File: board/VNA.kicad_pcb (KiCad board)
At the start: 2 copper layers, 100 x 100 mm, 129 parts, among them J1 Conn_02x05_Odd_Even, J10 Conn_01x01, J11 Conn_01x01, J12 Conn_01x01, J13 Barrel_Jack, J15 Conn_02x05_Odd_Even, J17 Conn_01x04, J18 Conn_01x01, J19 Conn_01x01, J2 Conn_Coaxial, J20 Conn_01x01, J21 Conn_01x01, J22 Conn_01x02, J3 Conn_01x01, J4 Conn_01x01, J5 Conn_01x01, J6 Conn_01x01, J7 Conn_01x01, J8 Conn_01x01, J9 Conn_Coaxial, Q1 SS9018, U1 SI5351A, U2 LM339, U3 SA612, U4 SA612, U5 SA612, U6 TL082, U7 TL082, U9 LM7805_TO220, Y1 27 MHz

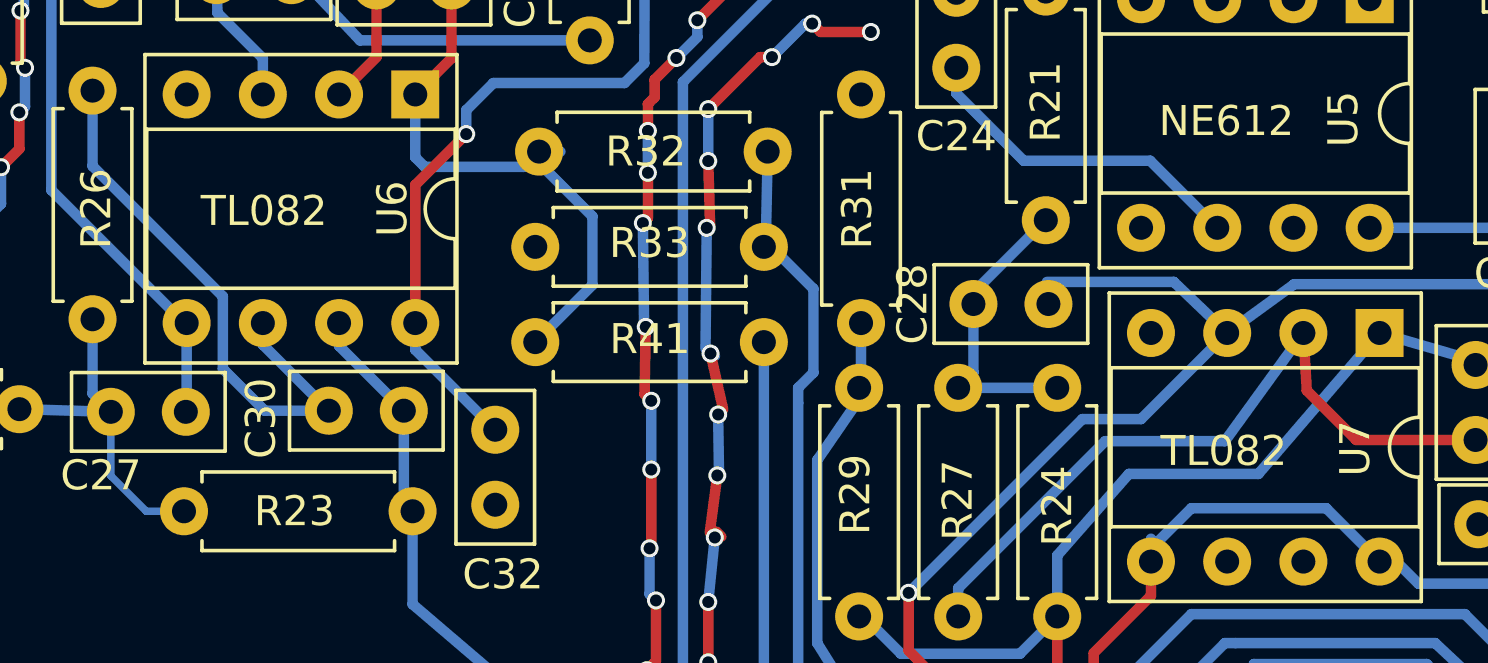
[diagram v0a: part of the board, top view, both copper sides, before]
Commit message: Changed TL082 to LM358, other corrections to software
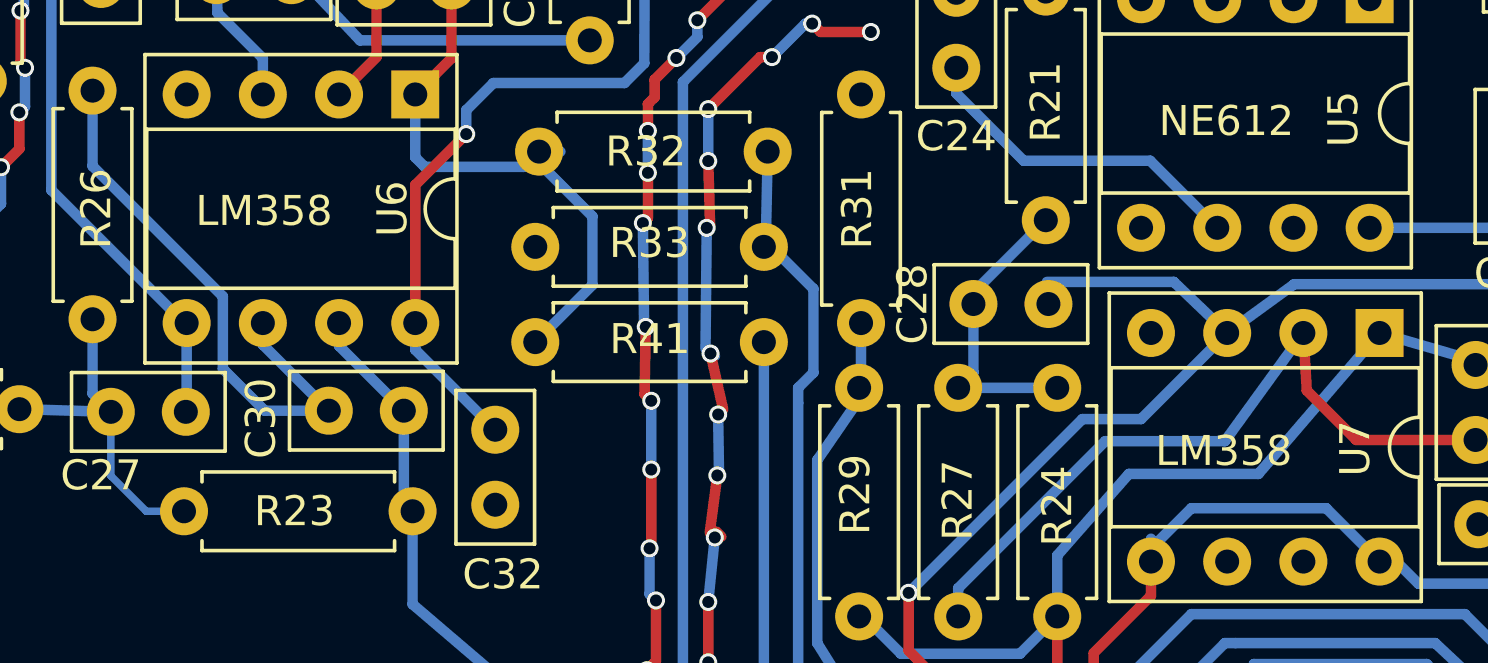
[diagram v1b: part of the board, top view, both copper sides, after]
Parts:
- R3: value 470R -> 1k
- R4: value 470R -> 680R
- R42: value 10k -> 1k
- U6, U7: value TL082 -> LM358
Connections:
- net 2V5 renamed 2V0
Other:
- board text added: "LM358"
- board text removed: "TL082"

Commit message: A few minor fixes, grounding, etc.
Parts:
- moved U9 4.05 mm to (145.9, 121.0)
- moved C38 0.56 mm to (145.8, 111.1)
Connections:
- J18 pad 1: (no net) -> GND
- J19 pad 1: (no net) -> GND
- J20 pad 1: (no net) -> GND
- J21 pad 1: (no net) -> GND
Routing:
- net +5V: track 310.8 -> 317.6 mm
- net Net-(C47-Pad1): track 43.3 -> 47.0 mm

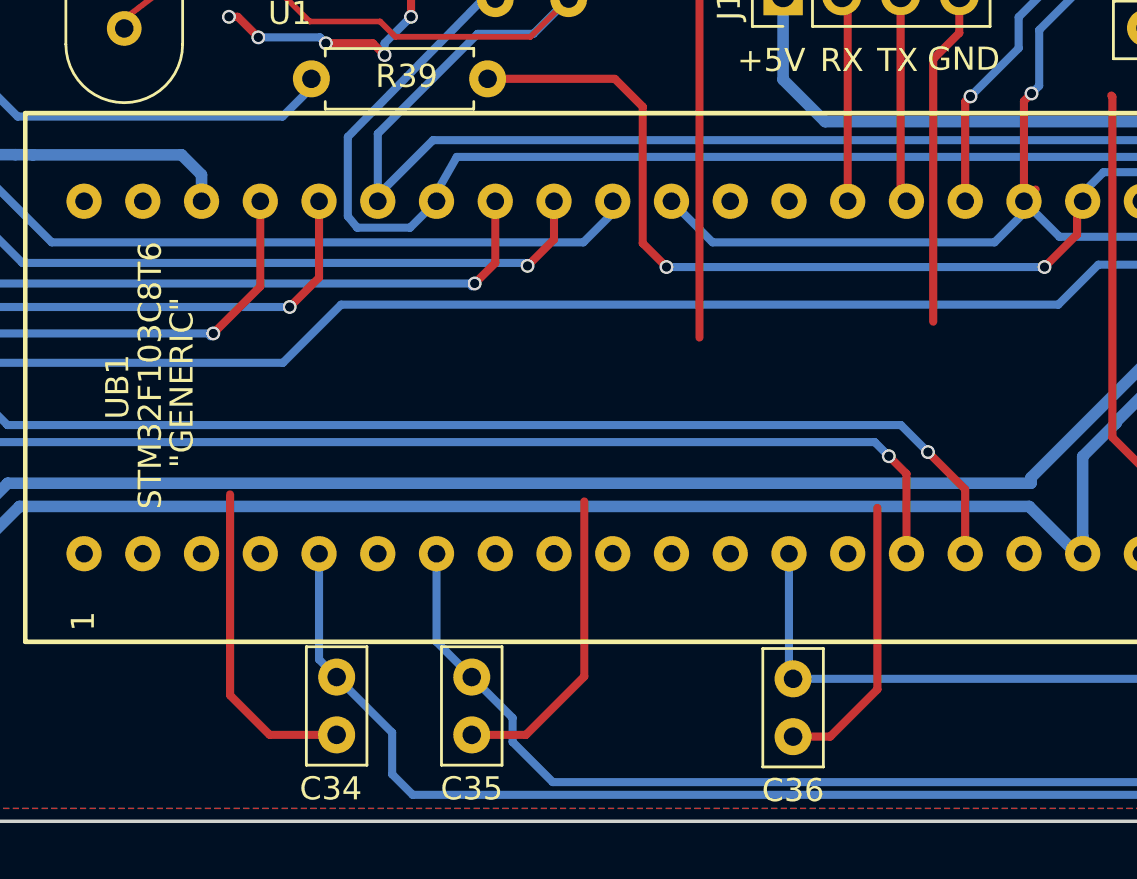
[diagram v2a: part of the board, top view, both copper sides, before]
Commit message: Added ground connections
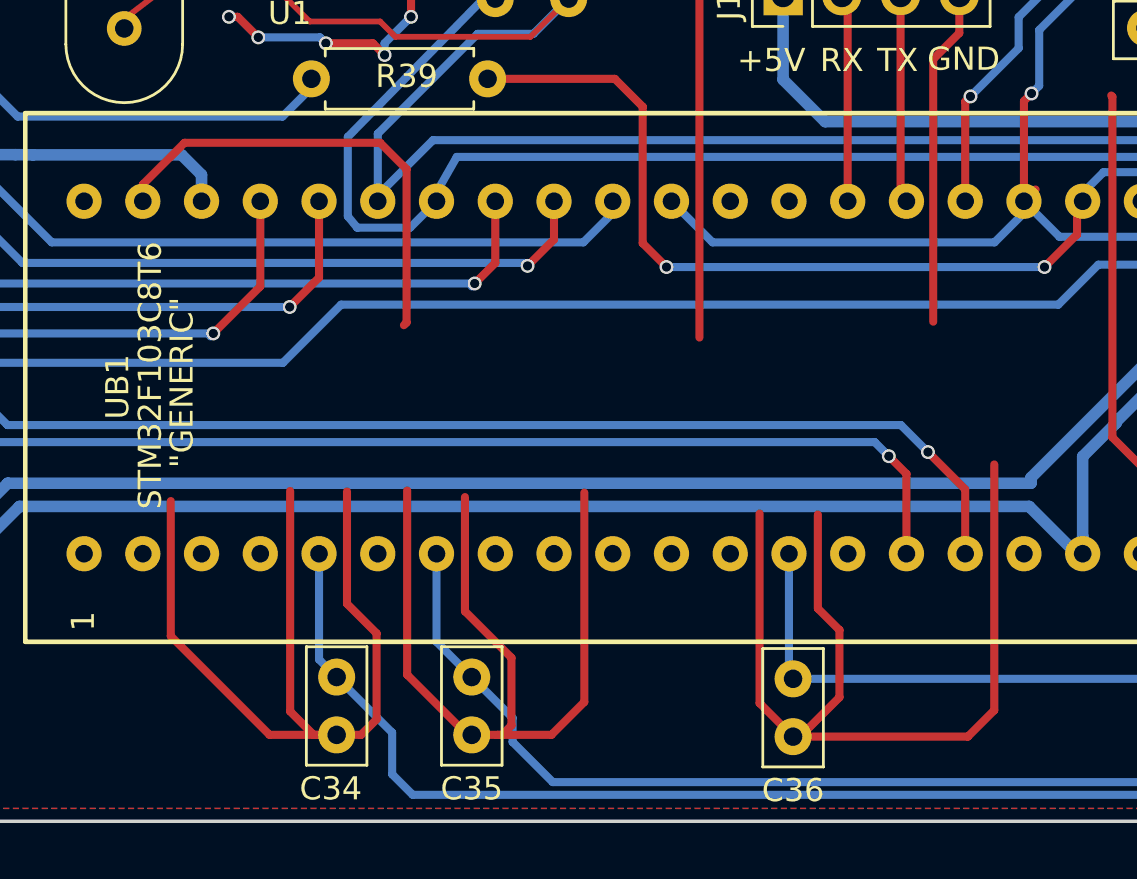
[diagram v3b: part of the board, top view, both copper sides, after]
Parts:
- R16: value 100R -> 51R
- R40: value NC -> 100R
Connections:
- UB1 pad 71: (no net) -> GND
- UB1 pad 74: (no net) -> GND
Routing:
- net GND: track 610.7 -> 709.1 mm
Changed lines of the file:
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@@
 (kicad_pcb (version 4) (host pcbnew 4.0.7)
   (general
-    (links 247)
+    (links 249)
     (no_connects 0)
     (area 48.252381 29.036639 153.343482 154.699701)
     (thickness 1.6)
     (drawings 35)
-    (tracks 1485)
+    (tracks 1515)
     (zones 0)
     (modules 129)
@@
   )
   (setup
-    (last_trace_width 0.25)
+    (last_trace_width 0.35)
     (user_trace_width 0.35)
     (user_trace_width 0.5)
@@
       (effects (font (size 1 1) (thickness 0.15)))
     )
-    (fp_text value 100R (at 3.81 2.31 270) (layer F.Fab)
+    (fp_text value 51R (at 3.81 2.31 270) (layer F.Fab)
       (effects (font (size 1 1) (thickness 0.15)))
     )
@@
     (pad 70 thru_hole circle (at -7.62 21.59 90) (size 1.524 1.524) (drill 0.762) (layers *.Cu *.Mask)
       (net 46 +3V3))
-    (pad 71 thru_hole circle (at -7.62 24.13 90) (size 1.524 1.524) (drill 0.762) (layers *.Cu *.Mask))
+    (pad 71 thru_hole circle (at -7.62 24.13 90) (size 1.524 1.524) (drill 0.762) (layers *.Cu *.Mask)
+      (net 2 GND))
     (pad 72 thru_hole circle (at -7.62 26.67 90) (size 1.524 1.524) (drill 0.762) (layers *.Cu *.Mask)
       (net 2 GND))
     (pad 73 thru_hole circle (at 7.62 -21.59 90) (size 1.524 1.524) (drill 0.762) (layers *.Cu *.Mask))
-    (pad 74 thru_hole circle (at 7.62 -19.05 90) (size 1.524 1.524) (drill 0.762) (layers *.Cu *.Mask))
+    (pad 74 thru_hole circle (at 7.62 -19.05 90) (size 1.524 1.524) (drill 0.762) (layers *.Cu *.Mask)
+      (net 2 GND))
     (pad 75 thru_hole circle (at 7.62 -16.51 90) (size 1.524 1.524) (drill 0.762) (layers *.Cu *.Mask)
       (net 45 +5V))
@@
       (effects (font (size 1 1) (thickness 0.15)))
     )
-    (fp_text value NC (at 3.81 2.31) (layer F.Fab)
+    (fp_text value 100R (at 3.81 2.31) (layer F.Fab)
       (effects (font (size 1 1) (thickness 0.15)))
     )
@@
   (segment (start 144.5768 76.962) (end 145.796 76.962) (width 0.5) (layer B.Cu) (net 1) (status 20))
   (segment (start 142.6464 78.8924) (end 144.5768 76.962) (width 0.5) (layer B.Cu) (net 1))
-  (segment (start 80.264 146.264) (end 77.36904 146.264) (width 0.35) (layer F.Cu) (net 2))
-  (segment (start 75.65644 144.5514) (end 75.65644 135.8646) (width 0.35) (layer F.Cu) (net 2))
-  (segment (start 77.36904 146.264) (end 75.65644 144.5514) (width 0.35) (layer F.Cu) (net 2))
-  (segment (start 99.9998 146.3402) (end 101.60444 146.3402) (width 0.35) (layer F.Cu) (net 2))
-  (segment (start 103.64724 144.2974) (end 103.64724 136.4488) (width 0.35) (layer F.Cu) (net 2))
-  (segment (start 101.60444 146.3402) (end 103.64724 144.2974) (width 0.35) (layer F.Cu) (net 2))
-  (segment (start 86.106 146.264) (end 88.44724 146.264) (width 0.35) (layer F.Cu) (net 2))
-  (segment (start 90.97264 143.7386) (end 90.97264 136.1694) (width 0.35) (layer F.Cu) (net 2))
-  (segment (start 88.44724 146.264) (end 90.97264 143.7386) (width 0.35) (layer F.Cu) (net 2))
+  (segment (start 71.882 123.19) (end 71.882 122.4661) (width 0.35) (layer F.Cu) (net 2))
+  (segment (start 71.882 122.4661) (end 73.6854 120.6627) (width 0.35) (layer F.Cu) (net 2))
+  (segment (start 73.6854 120.6627) (end 82.1436 120.6627) (width 0.35) (layer F.Cu) (net 2))
+  (segment (start 82.1436 120.6627) (end 83.2866 121.8057) (width 0.35) (layer F.Cu) (net 2))
+  (segment (start 83.2866 121.8057) (end 83.2866 128.4351) (width 0.35) (layer F.Cu) (net 2))
+  (segment (start 83.2866 128.4351) (end 83.1723 128.5494) (width 0.35) (layer F.Cu) (net 2))
+  (segment (start 80.264 146.264) (end 77.36396 146.264) (width 0.35) (layer F.Cu) (net 2))
+  (segment (start 73.09104 141.99108) (end 73.09104 136.15162) (width 0.35) (layer F.Cu) (net 2))
+  (segment (start 77.36396 146.264) (end 73.09104 141.99108) (width 0.35) (layer F.Cu) (net 2))
+  (segment (start 99.9998 146.3402) (end 107.5582 146.3402) (width 0.35) (layer F.Cu) (net 2))
+  (segment (start 108.6993 145.1991) (end 108.6993 134.5692) (width 0.35) (layer F.Cu) (net 2))
+  (segment (start 107.5582 146.3402) (end 108.6993 145.1991) (width 0.35) (layer F.Cu) (net 2))
+  (segment (start 87.20074 146.264) (end 89.5496 146.264) (width 0.35) (layer F.Cu) (net 2))
+  (segment (start 90.97264 144.84096) (end 90.97264 135.7884) (width 0.35) (layer F.Cu) (net 2))
+  (segment (start 89.5496 146.264) (end 90.97264 144.84096) (width 0.35) (layer F.Cu) (net 2))
+  (segment (start 99.9998 146.3402) (end 100.30396 146.3402) (width 0.35) (layer F.Cu) (net 2))
+  (segment (start 100.30396 146.3402) (end 102.0064 144.63776) (width 0.35) (layer F.Cu) (net 2))
+  (segment (start 101.07168 140.79728) (end 101.07168 136.73328) (width 0.35) (layer F.Cu) (net 2))
+  (segment (start 102.0064 141.732) (end 101.07168 140.79728) (width 0.35) (layer F.Cu) (net 2))
+  (segment (start 102.0064 144.63776) (end 102.0064 141.732) (width 0.35) (layer F.Cu) (net 2))
+  (segment (start 98.552 136.69264) (end 98.552 144.8924) (width 0.35) (layer F.Cu) (net 2))
+  (segment (start 98.552 144.8924) (end 99.9998 146.3402) (width 0.35) (layer F.Cu) (net 2))
+  (segment (start 85.81136 135.98144) (end 85.81136 140.9192) (width 0.35) (layer F.Cu) (net 2))
+  (segment (start 87.416 146.264) (end 87.20074 146.264) (width 0.35) (layer F.Cu) (net 2))
+  (segment (start 87.20074 146.264) (end 86.106 146.264) (width 0.35) (layer F.Cu) (net 2))
+  (segment (start 87.82304 145.85696) (end 87.416 146.264) (width 0.35) (layer F.Cu) (net 2))
+  (segment (start 87.82304 142.93088) (end 87.82304 145.85696) (width 0.35) (layer F.Cu) (net 2))
+  (segment (start 85.81136 140.9192) (end 87.82304 142.93088) (width 0.35) (layer F.Cu) (net 2))
+  (segment (start 86.106 146.264) (end 85.9136 146.264) (width 0.35) (layer F.Cu) (net 2))
+  (segment (start 85.9136 146.264) (end 83.312 143.6624) (width 0.35) (layer F.Cu) (net 2))
+  (segment (start 83.312 143.6624) (end 83.312 135.69696) (width 0.35) (layer F.Cu) (net 2))
+  (segment (start 80.264 146.264) (end 81.32 146.264) (width 0.35) (layer F.Cu) (net 2))
+  (segment (start 80.71104 140.59408) (end 80.71104 135.7376) (width 0.35) (layer F.Cu) (net 2))
+  (segment (start 81.9912 141.87424) (end 80.71104 140.59408) (width 0.35) (layer F.Cu) (net 2))
+  (segment (start 81.9912 145.5928) (end 81.9912 141.87424) (width 0.35) (layer F.Cu) (net 2))
+  (segment (start 81.32 146.264) (end 81.9912 145.5928) (width 0.35) (layer F.Cu) (net 2))
+  (segment (start 80.264 146.264) (end 79.26896 146.264) (width 0.35) (layer F.Cu) (net 2))
+  (segment (start 78.25232 145.24736) (end 78.25232 135.71728) (width 0.35) (layer F.Cu) (net 2))
+  (segment (start 79.26896 146.264) (end 78.25232 145.24736) (width 0.35) (layer F.Cu) (net 2))
   (segment (start 93.51264 106.1974) (end 93.51264 108.4834) (width 0.35) (layer F.Cu) (net 2))
   (segment (start 95.95104 110.9218) (end 95.95104 129.0828) (width 0.35) (layer F.Cu) (net 2))

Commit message: Changed SMA connector, added dual power option for LCD
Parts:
- added C41: 100 nF, Capacitors_THT:C_Disc_D5.0mm_W2.5mm_P2.50mm, F.Cu at (55.4, 140.5)
- added JP5: Jumper_NC_Dual, Pin_Headers:Pin_Header_Straight_1x03_Pitch2.54mm, F.Cu at (63.9, 141.6)
- added U8: LM1117-3.3, TO_SOT_Packages_THT:TO-220-3_Vertical, F.Cu at (74.5, 146.0)
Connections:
- J1 pad 1: +5V -> Net-(J1-Pad1)
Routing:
- net Net-(C41-Pad1): track 0.00 -> 20.1 mm
- net Net-(J1-Pad1): track 0.00 -> 7.02 mm
- net +5V: track 317.6 -> 320.0 mm
- net +3V3: track 179.5 -> 181.5 mm
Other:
- board text added: "3V3"
- board text added: "LM1117-3.3"
